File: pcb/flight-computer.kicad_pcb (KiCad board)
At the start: 4 copper layers, 83.7 x 62.9 mm, 82 parts, among them J1 MicroSD Slot, J2 USB_C_Receptacle_USB2.0_16P, J3 SMA_Coax, J4 Conn_01x02, J5 ARM, SW1 SW_Push, SW2 SW_Push, U1 RP2040, U10 LM3671MF, U11 TPS2116DRL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

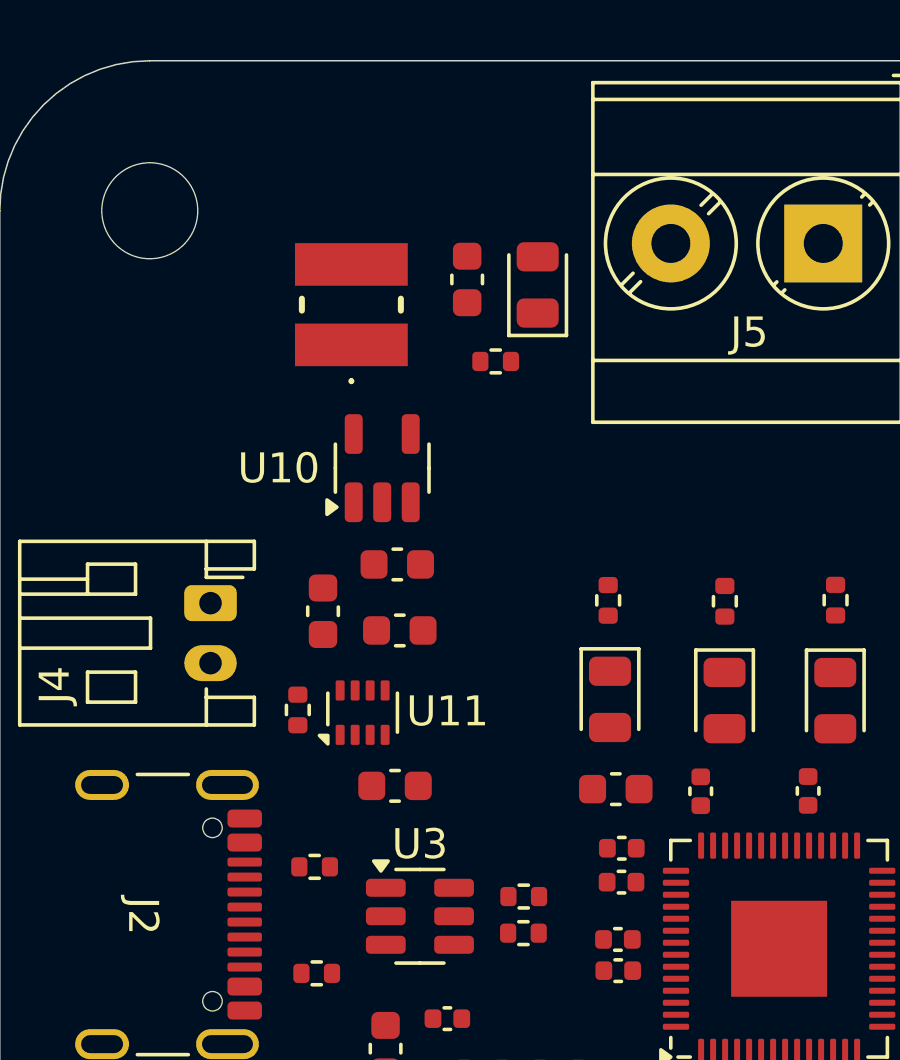
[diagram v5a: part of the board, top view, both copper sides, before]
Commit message: Added reverse polarity protection on JST connector
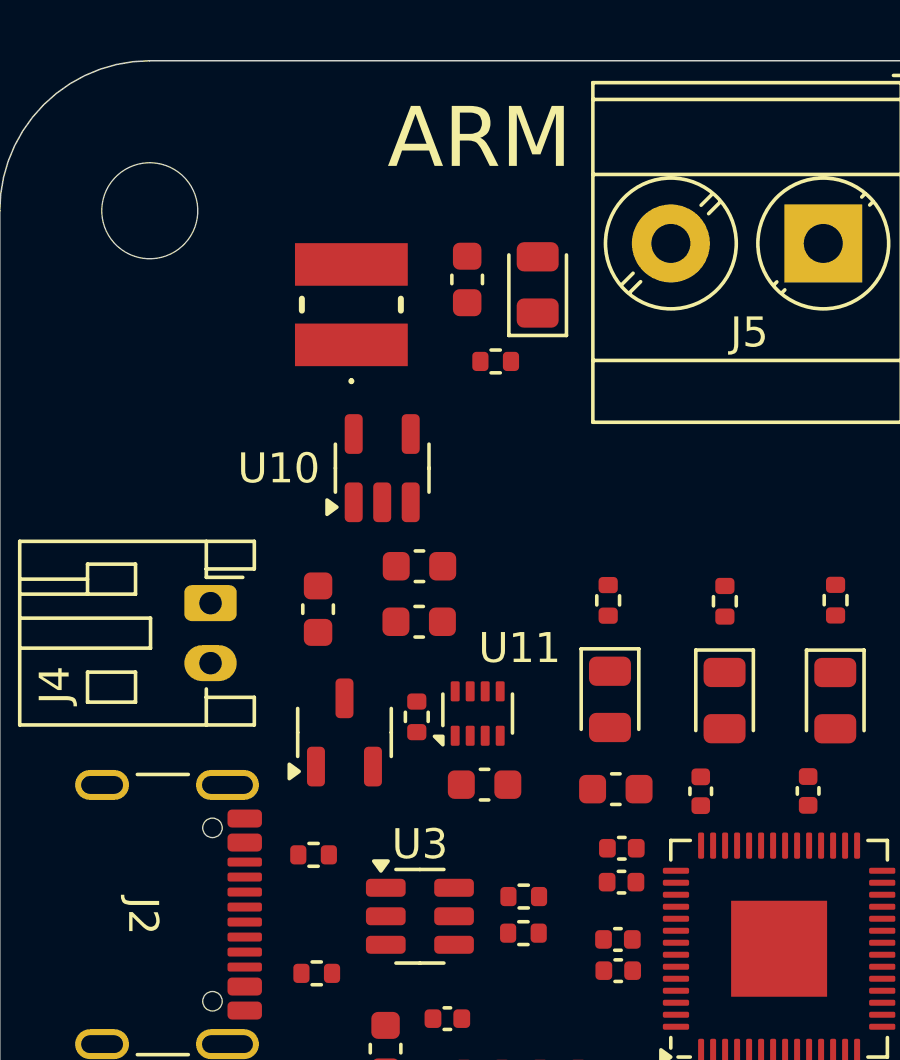
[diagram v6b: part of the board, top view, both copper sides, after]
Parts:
- added Q1: PMOS, Package_TO_SOT_SMD:SOT-23-3, F.Cu at (95.7, 93.0)
- moved R16 3.97 mm to (98.1, 92.5)
- moved U11 3.84 mm to (100.1, 92.4)
- moved C28 3.22 mm to (98.2, 89.3), turned to 180 degrees
- moved C29 2.99 mm to (100.3, 94.7)
- moved C32 2.82 mm to (94.8, 88.9), turned to 90 degrees
- moved C31 0.74 mm to (98.2, 87.5)
- moved R10 0.40 mm to (94.7, 97.1)
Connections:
- J4 pad 2: +3V7 -> /Power/BAT+
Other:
- board text added: "ARM"

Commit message: Almost done routing
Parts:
- moved R1 5.02 mm to (88.9, 121.5)
- moved D1 2.06 mm to (105.7, 90.2)
- moved D3 2.06 mm to (113.2, 90.2)
- moved R12 2.06 mm to (105.6, 86.9)
- moved R13 2.06 mm to (109.5, 86.9)
- moved D2 2.06 mm to (109.5, 90.2)
- moved R14 2.06 mm to (113.2, 86.9)
- moved SW2 1.90 mm to (89.6, 117.6), turned to 180 degrees
- moved C19 1.05 mm to (97.1, 120.4)
- moved R6 1.05 mm to (96.6, 118.2)
- moved U4 1.05 mm to (102.0, 119.0)
- moved R5 1.05 mm to (96.6, 116.8)
- moved C11 1.01 mm to (111.2, 106.6)
- moved C6 0.88 mm to (104.0, 101.1)
- moved C13 0.84 mm to (104.0, 100.0)
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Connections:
- net Net-(U1-USB_DM) renamed /RD-
- net Net-(U1-USB_DP) renamed /RD+
- net Net-(U10-SW) renamed /Power/NSY_OUT
- Q1 pad 1: /Power/BAT+ -> GND
- Q1 pad 2: GND -> +3V7
- Q1 pad 3: +3V7 -> /Power/BAT+
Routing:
- net GND: track 0.00 -> 268.0 mm, vias 0 -> 78
- net +3V3: track 0.00 -> 90.1 mm, vias 0 -> 28
- net I2C0_SCL: track 0.00 -> 72.4 mm, vias 0 -> 2
- net I2C0_SDA: track 0.00 -> 62.4 mm, vias 0 -> 2
- net MCU_UART1_TX: track 0.00 -> 39.6 mm
- net MCU_UART1_RX: track 0.00 -> 38.5 mm
- net MCU_UART0_TX: track 0.00 -> 27.3 mm, vias 0 -> 2
- net MCU_UART0_RX: track 0.00 -> 26.8 mm, vias 0 -> 2
- net /Power/REGULATOR_IN: track 0.00 -> 25.8 mm, vias 0 -> 2
- net I2C1_SCL: track 0.00 -> 24.3 mm, vias 0 -> 2
- net /BUZZ: track 0.00 -> 23.9 mm
- net +5V: track 0.00 -> 23.7 mm
- net /QSPI_SS: track 0.00 -> 21.5 mm
- net I2C1_SDA: track 0.00 -> 21.5 mm, vias 0 -> 2
- net /Power/PWR_SRC: track 0.00 -> 20.8 mm
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- added copper zone on F.Cu, net +3V3
- added copper zone on F.Cu, net /Power/NSY_OUT

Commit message: Added test points and finished routing
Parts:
- added 3V3: TestPoint, TestPoint:TestPoint_Pad_D1.5mm, F.Cu at (89.1, 117.1)
- added 3V7: TestPoint, TestPoint:TestPoint_Pad_D1.5mm, F.Cu at (103.0, 89.6)
- added 5V: TestPoint, TestPoint:TestPoint_Pad_D1.0mm, F.Cu at (97.2, 95.9)
- added BAT: TestPoint, TestPoint:TestPoint_Pad_D1.5mm, F.Cu at (88.6, 83.7)
- added GND: TestPoint, TestPoint:TestPoint_Pad_D1.5mm, F.Cu at (89.1, 121.2)
- added PWR: TestPoint, TestPoint:TestPoint_Pad_D1.5mm, F.Cu at (102.0, 85.8)
- added REF**: OSHW-Logo_7.5x8mm_SilkScreen, Symbol:OSHW-Logo_7.5x8mm_SilkScreen, F.Cu at (162.1, 120.0)
- moved R1 55.3 mm to (117.4, 74.2)
- moved RST 49.8 mm to (117.6, 76.5)
- moved G*** 1.62 mm to (162.1, 110.3)
- moved D2 0.51 mm to (109.0, 90.0)
- moved R13 0.51 mm to (109.0, 86.7)
- moved C6 0.20 mm to (103.8, 101.2)
- moved C13 0.20 mm to (103.8, 100.1)
- moved R15 0.11 mm to (120.1, 78.5)
- renumbered SW1 to BOOT, SW2 to RST
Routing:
- net RST_N: track 2.47 -> 75.6 mm, vias 0 -> 2
- net GND: track 268.0 -> 297.5 mm, vias 78 -> 85
- net /Power/BAT+: track 5.70 -> 14.9 mm
- net +1V1: track 4.37 -> 8.27 mm
- net +3V3: track 90.1 -> 93.8 mm, vias 28 -> 36
- net +3V7: track 12.7 -> 15.0 mm
- net I2C0_SCL: track 72.4 -> 73.0 mm
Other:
- board text added: "+"
- board text added: "-"
- board text added: "ARMED"
- board text added: "EJECT"
- board text added: "Matteo Golin"
- board text added: "PANIC"
- board text added: "SHORT TO ARM"
- board text added: "START"
